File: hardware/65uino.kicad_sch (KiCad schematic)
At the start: 78 parts, among them J1 Barrel, J2 GPCO, J3 OLED, J4 USB2.0_16P, J5 Databus, J6 Chip select, J7 Addressbus, J8 Signals, SW1 RST, SW2 BTN, U1 R6507, U2 74HC161, U3 6532, U4 w27C512, U5 MIC5504-3.3YM5, U6 AMS1117-5.0, U7 SN74LVC1G14DBVR, U8 CH340G, U9 74HC138, X1 8MHz, Y2 12MHz

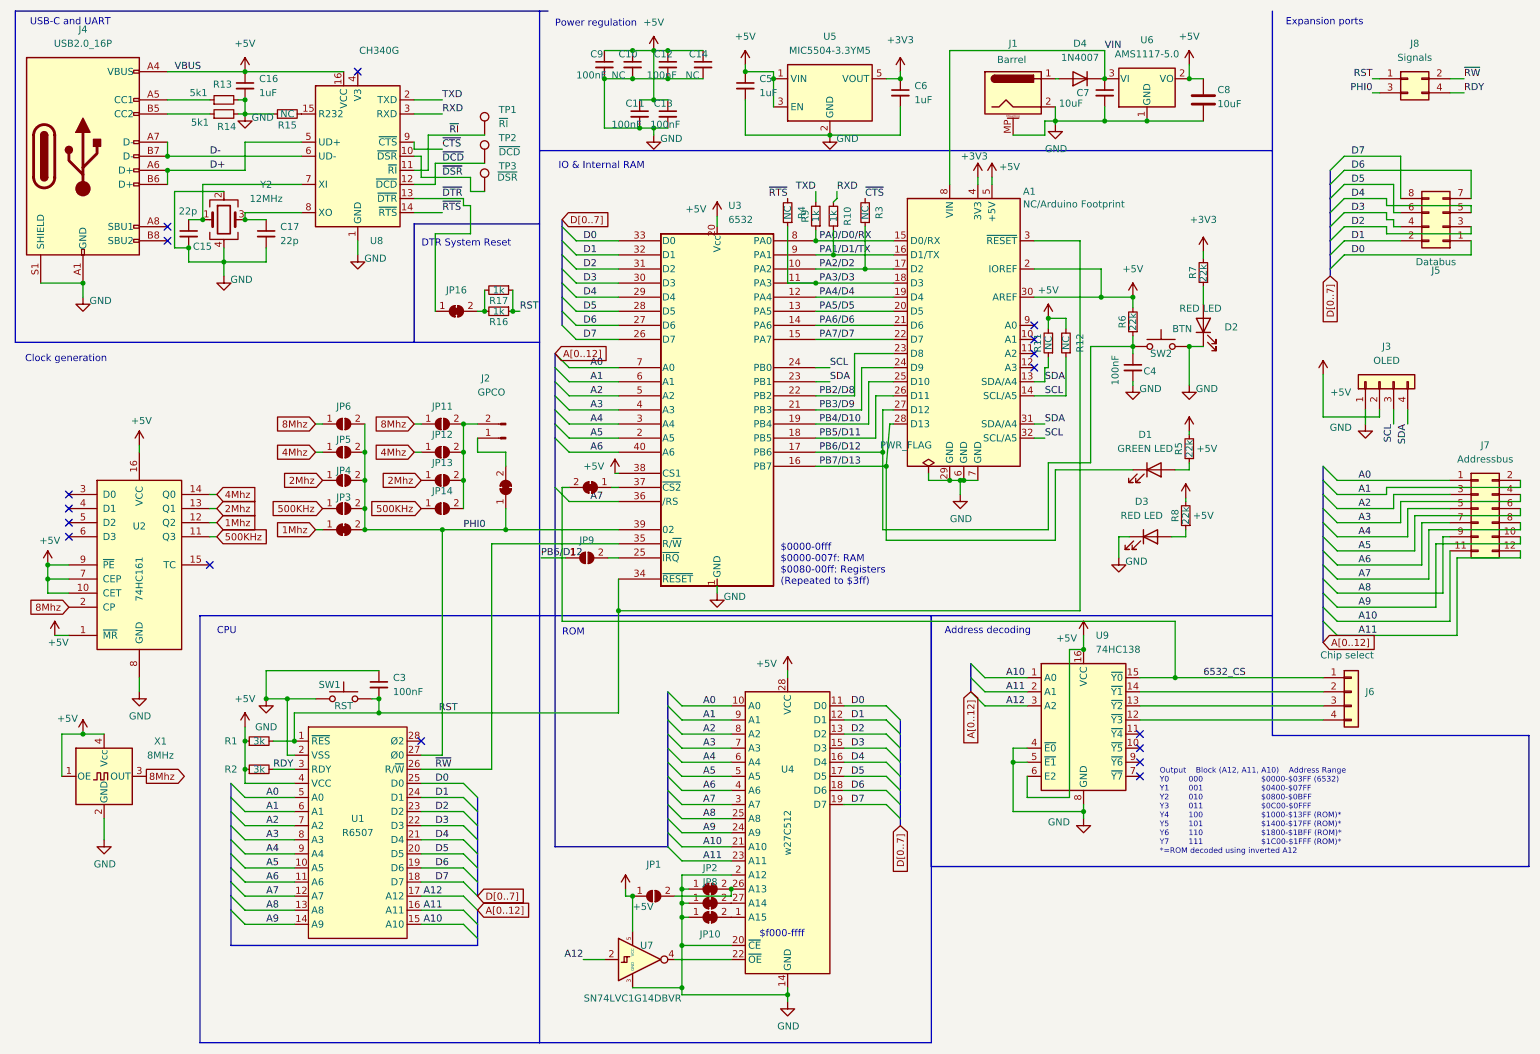
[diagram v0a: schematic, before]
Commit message: Rev 1.1
Rev 1.1 - working i2c scanner, default baud rate 4800, SOT23 EEPROM added
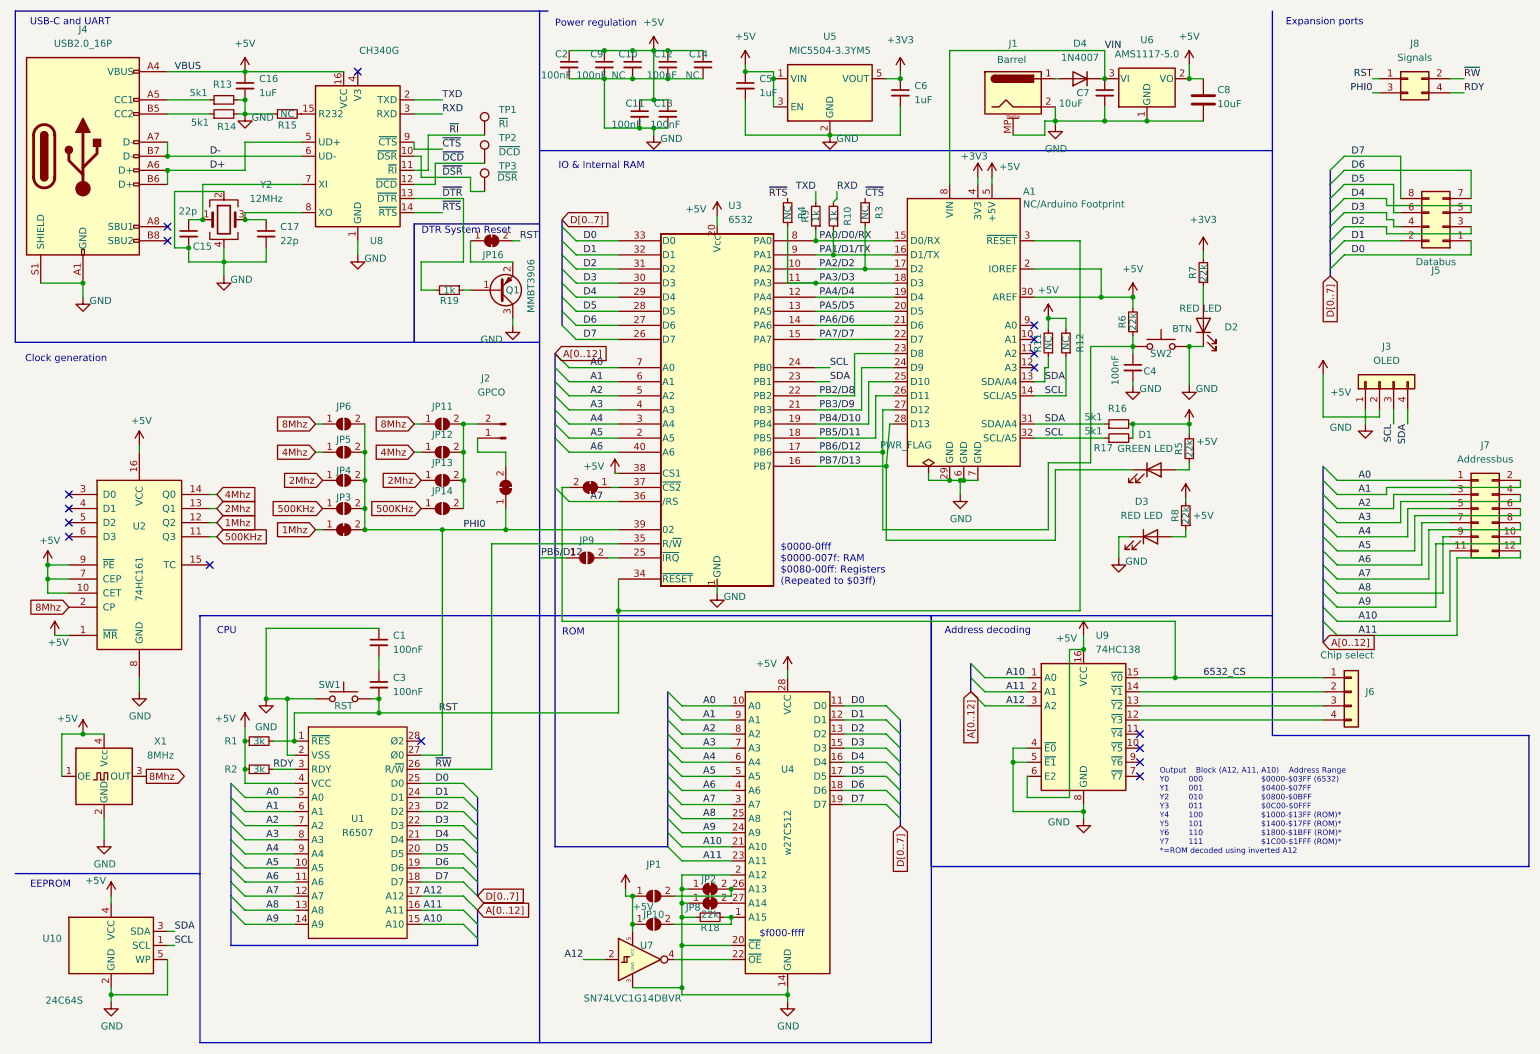
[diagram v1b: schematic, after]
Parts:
- removed JP10: SolderJumper_2_Bridged, Jumper:SolderJumper-2_P1.3mm_Bridged_RoundedPad1.0x1.5mm, symbol Jumper:SolderJumper_2_Bridged
- added C1, C2: 100nF, Capacitor_SMD:C_0805_2012Metric, symbol Device:C_Small
- added JP10: Jumper, Connector_PinHeader_2.54mm:PinHeader_1x02_P2.54mm_Vertical, symbol Jumper:SolderJumper_2_Open
- added Q1: MMBT3906, Package_TO_SOT_SMD:SOT-23, symbol Transistor_BJT:MMBT3906
- added R18: 22k, Resistor_SMD:R_0805_2012Metric, symbol Device:R_Small
- added R19: 1k, Resistor_SMD:R_0805_2012Metric, symbol Device:R_Small
- added U10: 24C64S, Package_TO_SOT_SMD:SOT-23-5, symbol Memory_EEPROM:AT24CS32-STUM
- R16, R17: value 1k -> 5k1
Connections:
- net +5V: now also R16.2, R17.2, C2.1, JP10.1 (A), U10.4 (VCC)
- net GND: now also C1.1, C2.2, Q1.3 (C), R18.2, U10.2 (GND), U10.5 (WP); no longer C3.1
- net RST: now also JP16.2 (B); no longer R16.1, R17.1
- net SCL: now also R17.1, U10.1 (SCL)
- net SDA: now also R16.1, U10.3 (SDA)
- net ~{DTR}: now also R19.2; no longer JP16.1 (A)
- net at U4.1 (A15): now also JP10.2 (B), R18.1
- new net: C1.2, C3.1
- new net: Q1.1 (B), R19.1
- new net: JP16.1 (A), Q1.2 (E)
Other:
- note added: "$0000-0fff $0000-007f: RAM $0080-00ff: Registers (Repeated to $03ff)"
- note added: "EEPROM"
- note removed: "$0000-0fff $0000-007f: RAM $0080-00ff: Registers (Repeated to $3ff)"
- moved on the sheet: JP16
